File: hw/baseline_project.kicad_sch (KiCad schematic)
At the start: 20 parts, among them J101 EXT_3V3, Q101 IRLD024PBF, SW101 UP, SW102 DOWN, SW103 LEFT, SW104 RIGHT, SW105 MODE, U101 EK-TM4C123GXL, U102 ESP8266-1, U103 Adafruit ST7735R

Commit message: added headers to files and modified Kicad
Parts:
- removed SW104: RIGHT, Button_Switch_THT:SW_PUSH_6mm, symbol Switch:SW_Push
- removed SW105: MODE, Button_Switch_THT:SW_PUSH_6mm, symbol Switch:SW_Push
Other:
- moved on the sheet: D101, LS101, Q101, R102, SW101, SW102, SW103, U103

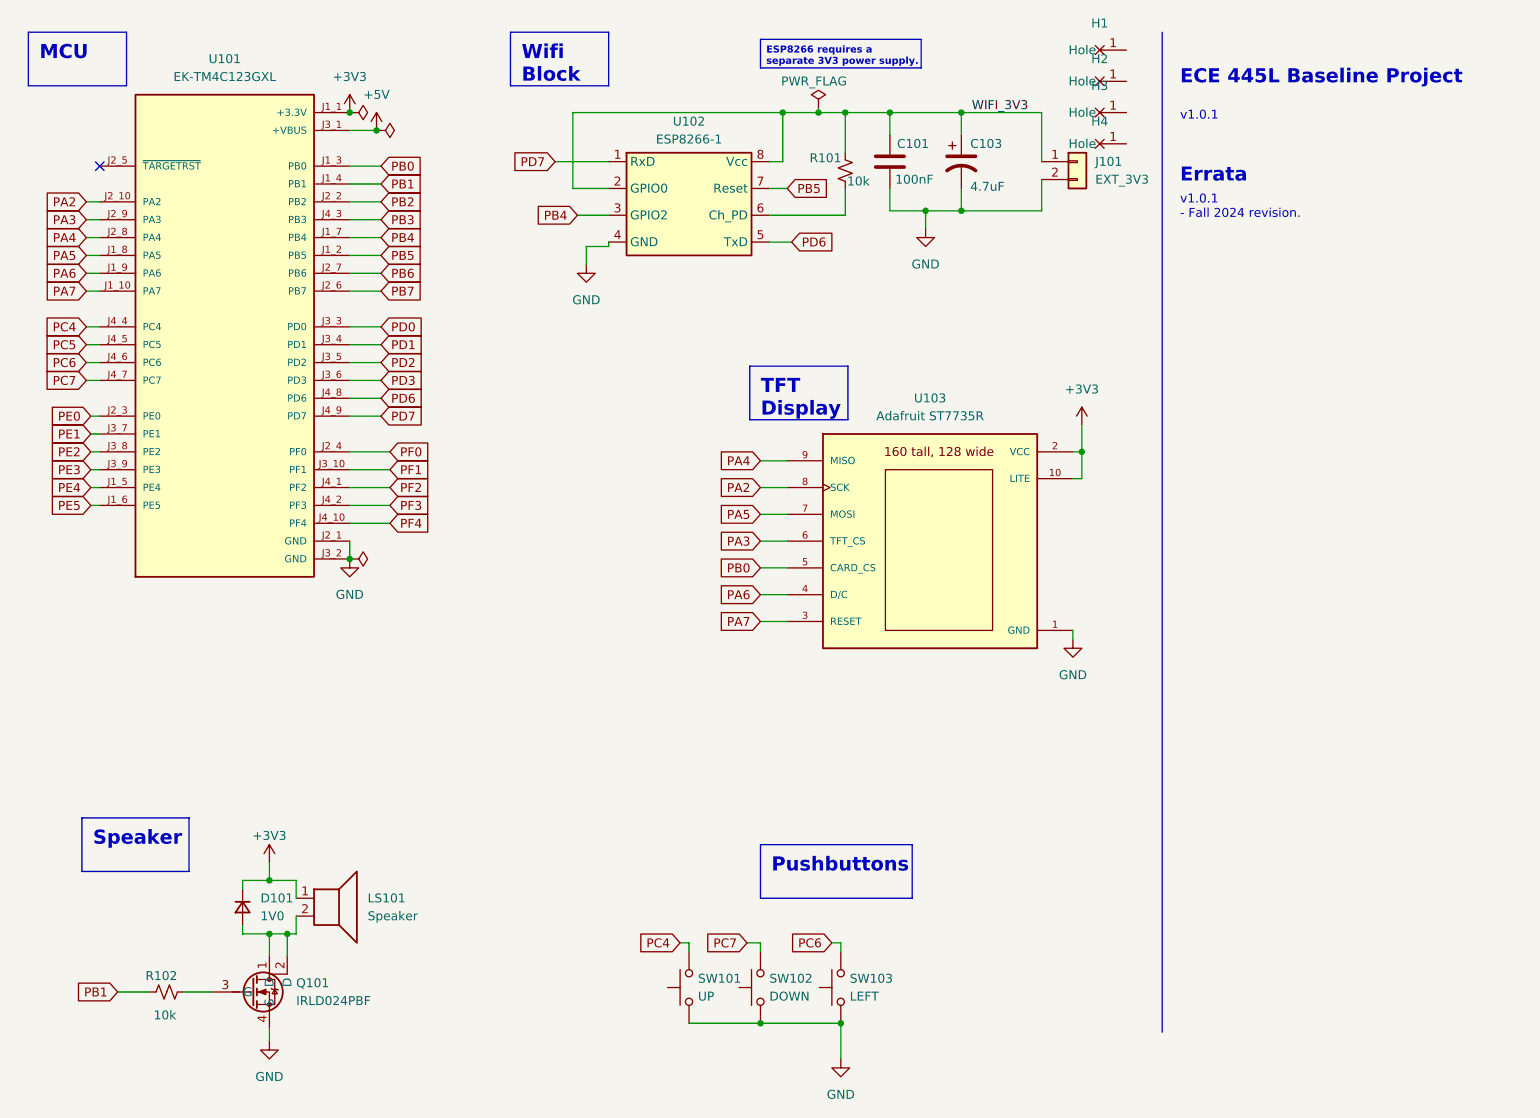
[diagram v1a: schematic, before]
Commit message: updated Kicad schematic to proper pins and propper LCD Screen
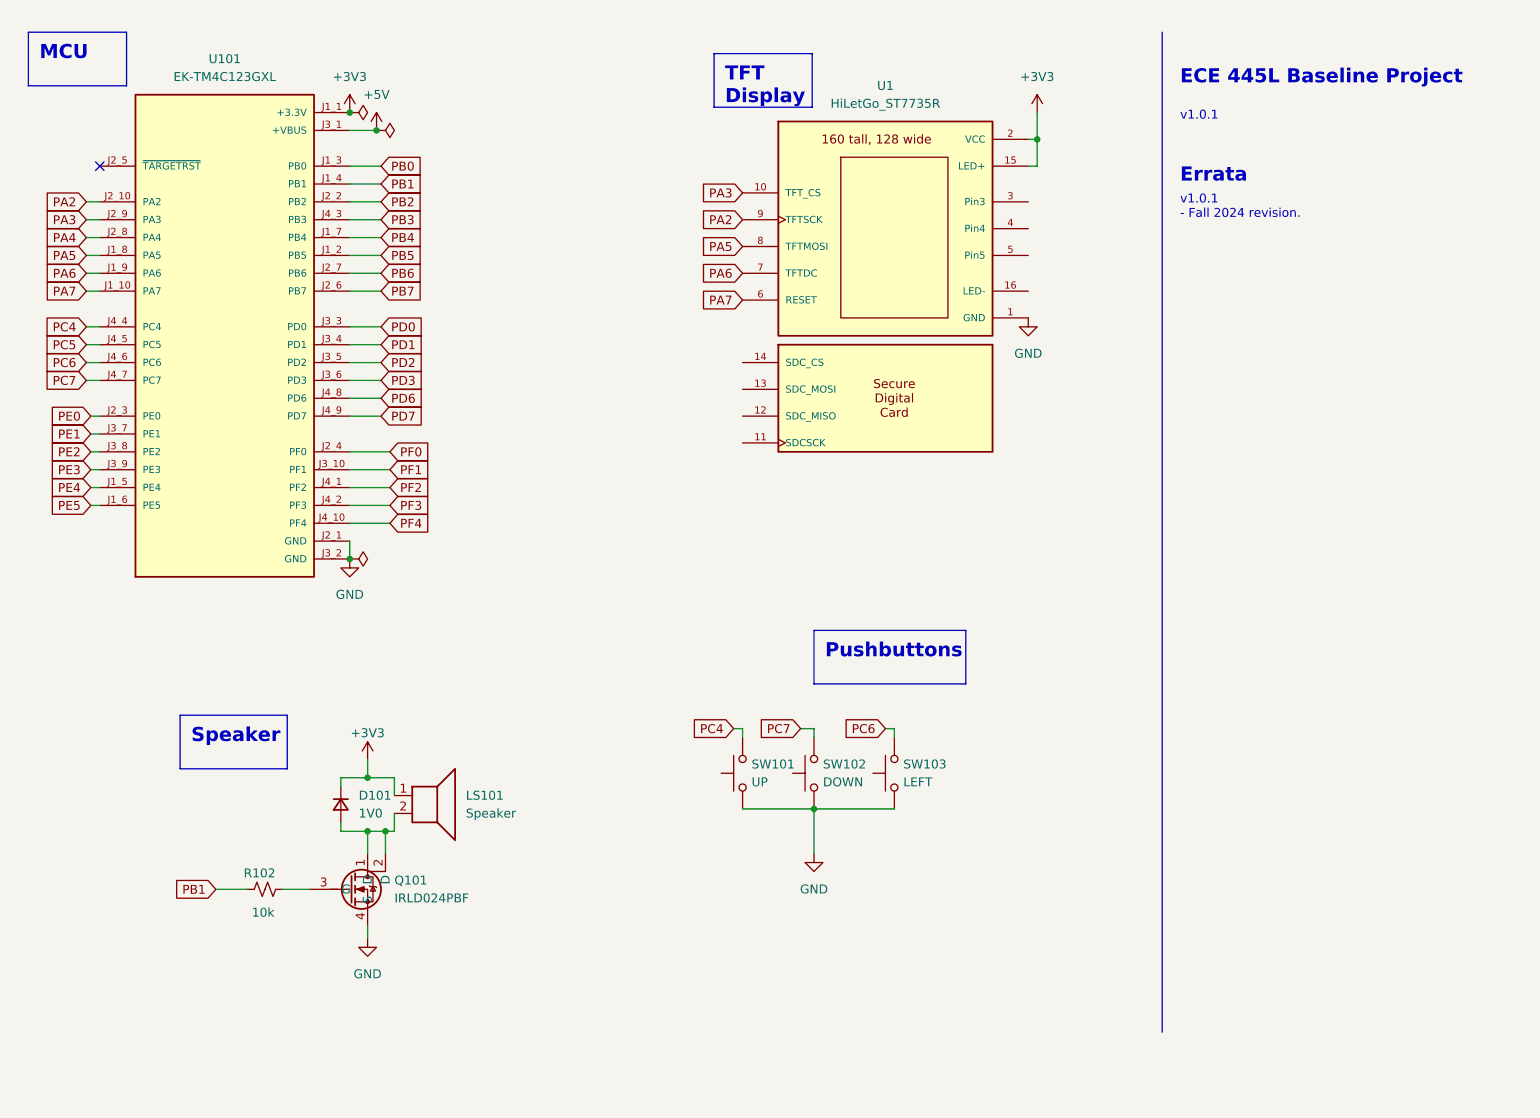
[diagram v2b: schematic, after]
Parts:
- removed C101: 100nF, ECE445L:C_Axial_200mil, symbol ECE445L:C
- removed C103: 4.7uF, ECE445L:CP_Radial_Tantal200mil, symbol ECE445L:C_Polarized
- removed H1, H2, H3, H4: ~, ECE445L:MountingHole_4_40, symbol ECE445L:MountingHole
- removed J101: EXT_3V3, Connector_Samtec_HPM_THT:Samtec_HPM-02-01-x-S_Straight_1x02_Pitch5.08mm, symbol Connector_Generic:Conn_01x02
- removed R101: 10k, ECE445L:R_Axial_DIN0204_L3.6mm_D1.6mm_P7.62mm_Horizontal, symbol ECE445L:R_0.125W
- removed U102: ESP8266-1, ECE445L:PinHeader_2x04_P2.54mm_Vertical, symbol ECE445L:ESP8266-1
- removed U103: Adafruit ST7735R, ECE445L:adafruit_st7735r2, symbol ECE445L:Adafruit_ST7735R
- added U1: HiLetGo_ST7735R, ECE445L:hiletgo_st7735r, symbol ECE445L:HiLetGo_ST7735R
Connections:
- net +3V3: now also U1.15 (LED+), U1.2 (VCC)
- net GND: now also U1.1 (GND)
- net PA2: now also U1.9 (TFTSCK)
- net PA3: now also U1.10 (TFT_CS)
- net PA5: now also U1.8 (TFTMOSI)
- net PA6: now also U1.7 (TFTDC)
- net PA7: now also U1.6 (RESET)
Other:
- moved on the sheet: D101, LS101, Q101, R102, SW101, SW102, SW103

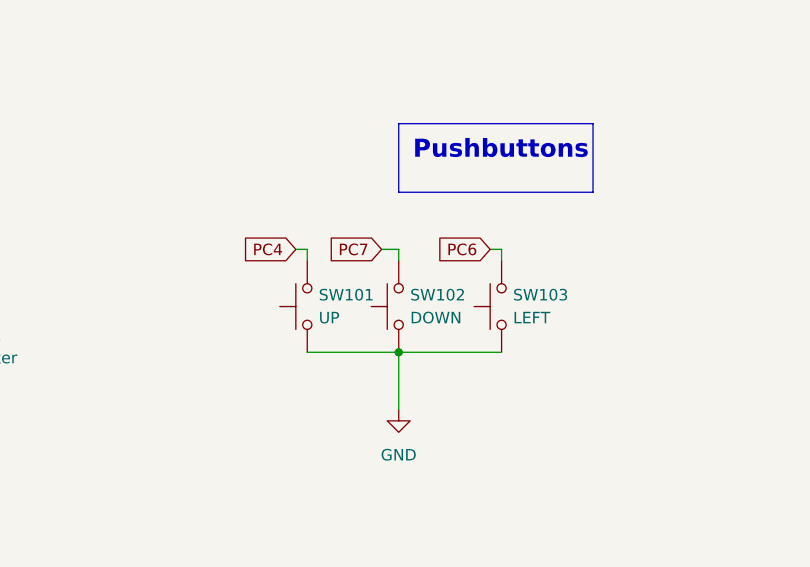
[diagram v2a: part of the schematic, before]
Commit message: added button initialization and headers to all .c files, also changed button layout for buttons on Kicad
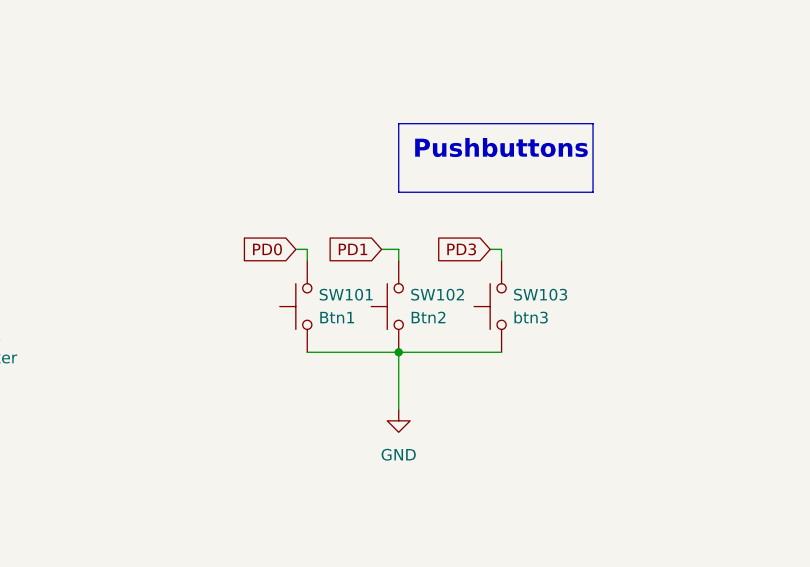
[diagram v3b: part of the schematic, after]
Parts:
- SW101: value UP -> Btn1
- SW102: value DOWN -> Btn2
- SW103: value LEFT -> btn3
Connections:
- net PC4: no longer SW101.2
- net PC6: no longer SW103.2
- net PC7: no longer SW102.2
- net PD0: now also SW101.2
- net PD1: now also SW102.2
- net PD3: now also SW103.2
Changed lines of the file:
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@@
 		)
 	)
-	(global_label "PC7"
+	(global_label "PD1"
 		(shape input)
 		(at 125.095 114.3 180)
@@
 		)
 	)
-	(global_label "PC4"
+	(global_label "PD0"
 		(shape input)
 		(at 115.57 114.3 180)
@@
 		)
 	)
-	(global_label "PC6"
+	(global_label "PD3"
 		(shape input)
 		(at 137.16 114.3 180)
@@
 		(fields_autoplaced yes)
 		(property "Reference" "SW101"
-			(at 118.11 119.38 90)
-			(effects
-				(font
-					(size 1.27 1.27)
-				)
-				(justify right)
-			)
-		)
-		(property "Value" "UP"
-			(at 118.11 121.92 90)
+			(at 118.11 119.3799 90)
+			(effects
+				(font
+					(size 1.27 1.27)
+				)
+				(justify right)
+			)
+		)
+		(property "Value" "Btn1"
+			(at 118.11 121.9199 90)
 			(effects
 				(font
@@
 		(fields_autoplaced yes)
 		(property "Reference" "SW102"
-			(at 128.27 119.38 90)
-			(effects
-				(font
-					(size 1.27 1.27)
-				)
-				(justify right)
-			)
-		)
-		(property "Value" "DOWN"
-			(at 128.27 121.92 90)
+			(at 128.27 119.3799 90)
+			(effects
+				(font
+					(size 1.27 1.27)
+				)
+				(justify right)
+			)
+		)
+		(property "Value" "Btn2"
+			(at 128.27 121.9199 90)
 			(effects
 				(font
@@
 		(fields_autoplaced yes)
 		(property "Reference" "SW103"
-			(at 139.7 119.38 90)
-			(effects
-				(font
-					(size 1.27 1.27)
-				)
-				(justify right)
-			)
-		)
-		(property "Value" "LEFT"
-			(at 139.7 121.92 90)
-			(effects
-				(font
+			(at 139.7 119.3799 90)
+			(effects
+				(font
+					(size 1.27 1.27)
+				)
+				(justify right)
+			)
+		)
+		(property "Value" "btn3"
+			(at 139.7 121.9199 90)
+			(effects
+				(font

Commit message: fixed and completed Kicad schematic
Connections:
- net +3V3: now also SW101.1, SW102.1, SW103.1
- net GND: no longer SW101.1, SW102.1, SW103.1
- net PD2: now also SW103.2
- net PD3: no longer SW103.2
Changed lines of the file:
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@@
 		)
 	)
-	(global_label "PD3"
+	(global_label "PD2"
 		(shape input)
 		(at 137.16 114.3 180)
@@
 	)
 	(symbol
-		(lib_id "power:GND")
-		(at 127 132.08 0)
-		(unit 1)
-		(exclude_from_sim no)
-		(in_bom yes)
-		(on_board yes)
-		(dnp no)
-		(fields_autoplaced yes)
-		(property "Reference" "#PWR0107"
-			(at 127 138.43 0)
-			(effects
-				(font
-					(size 1.27 1.27)
-				)
-				(hide yes)
-			)
-		)
-		(property "Value" "GND"
-			(at 127 137.16 0)
-			(effects
-				(font
-					(size 1.27 1.27)
-				)
-			)
-		)
-		(property "Footprint" ""
-			(at 127 132.08 0)
-			(effects
-				(font
-					(size 1.27 1.27)
-				)
-				(hide yes)
-			)
-		)
-		(property "Datasheet" ""
-			(at 127 132.08 0)
-			(effects
-				(font
-					(size 1.27 1.27)
-				)
-				(hide yes)
-			)
-		)
-		(property "Description" "Power symbol creates a global label with name \"GND\" , ground"
-			(at 127 132.08 0)
-			(effects
-				(font
-					(size 1.27 1.27)
-				)
-				(hide yes)
-			)
-		)
-		(pin "1"
-		)
-		(instances
-			(project "baseline_project"
-				(path "/69b823fd-c065-40ff-9bb9-c5835555f3eb"
-					(reference "#PWR0107")
-					(unit 1)
-				)
-			)
-		)
-	)
-	(symbol
 		(lib_id "Switch:SW_Push")
 		(at 127 120.65 90)
@@
 					(unit 1)
 				)
+			)
+		)
+	)
+	(symbol
+		(lib_id "power:+3V3")
+		(at 127 132.08 180)
+		(unit 1)
+		(exclude_from_sim no)
+		(in_bom yes)
+		(on_board yes)
+		(dnp no)
+		(fields_autoplaced yes)
+		(property "Reference" "#PWR01"
+			(at 127 128.27 0)
+			(effects
+				(font
+					(size 1.27 1.27)
+				)
+				(hide yes)
+			)
+		)
+		(property "Value" "+3V3"
+			(at 127 137.16 0)
+			(effects
+				(font
+					(size 1.27 1.27)
+				)
+			)
+		)
+		(property "Footprint" ""
+			(at 127 132.08 0)
+			(effects
+				(font
+					(size 1.27 1.27)
+				)
+				(hide yes)
+			)
+		)
+		(property "Datasheet" ""
+			(at 127 132.08 0)
+			(effects
+				(font
+					(size 1.27 1.27)
+				)
+				(hide yes)
+			)
+		)
+		(property "Description" "Power symbol creates a global label with name \"+3V3\""
+			(at 127 132.08 0)
+			(effects
+				(font
+					(size 1.27 1.27)
+				)
+				(hide yes)
+			)
+		)
+		(pin "1"
+		)
+		(instances
+			(project "baseline_project"
+				(path "/69b823fd-c065-40ff-9bb9-c5835555f3eb"
+					(reference "#PWR01")
+					(unit 1)
+				)
